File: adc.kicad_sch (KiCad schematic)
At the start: 15 parts, among them U9 ADS8584S

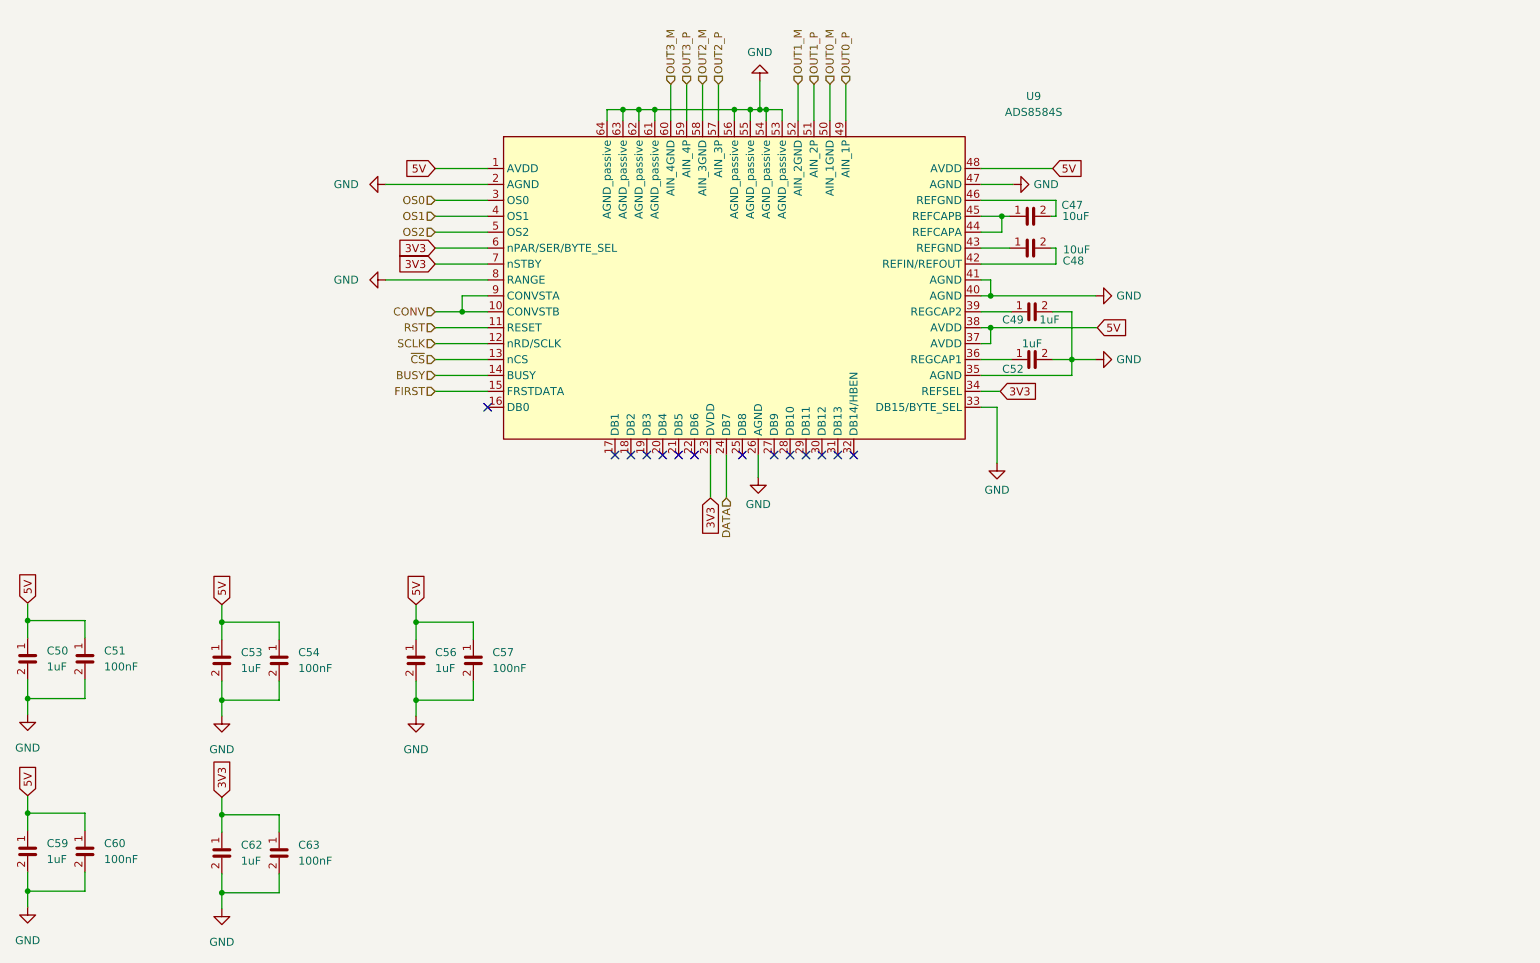
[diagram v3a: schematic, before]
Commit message: Added connector to all sheets.
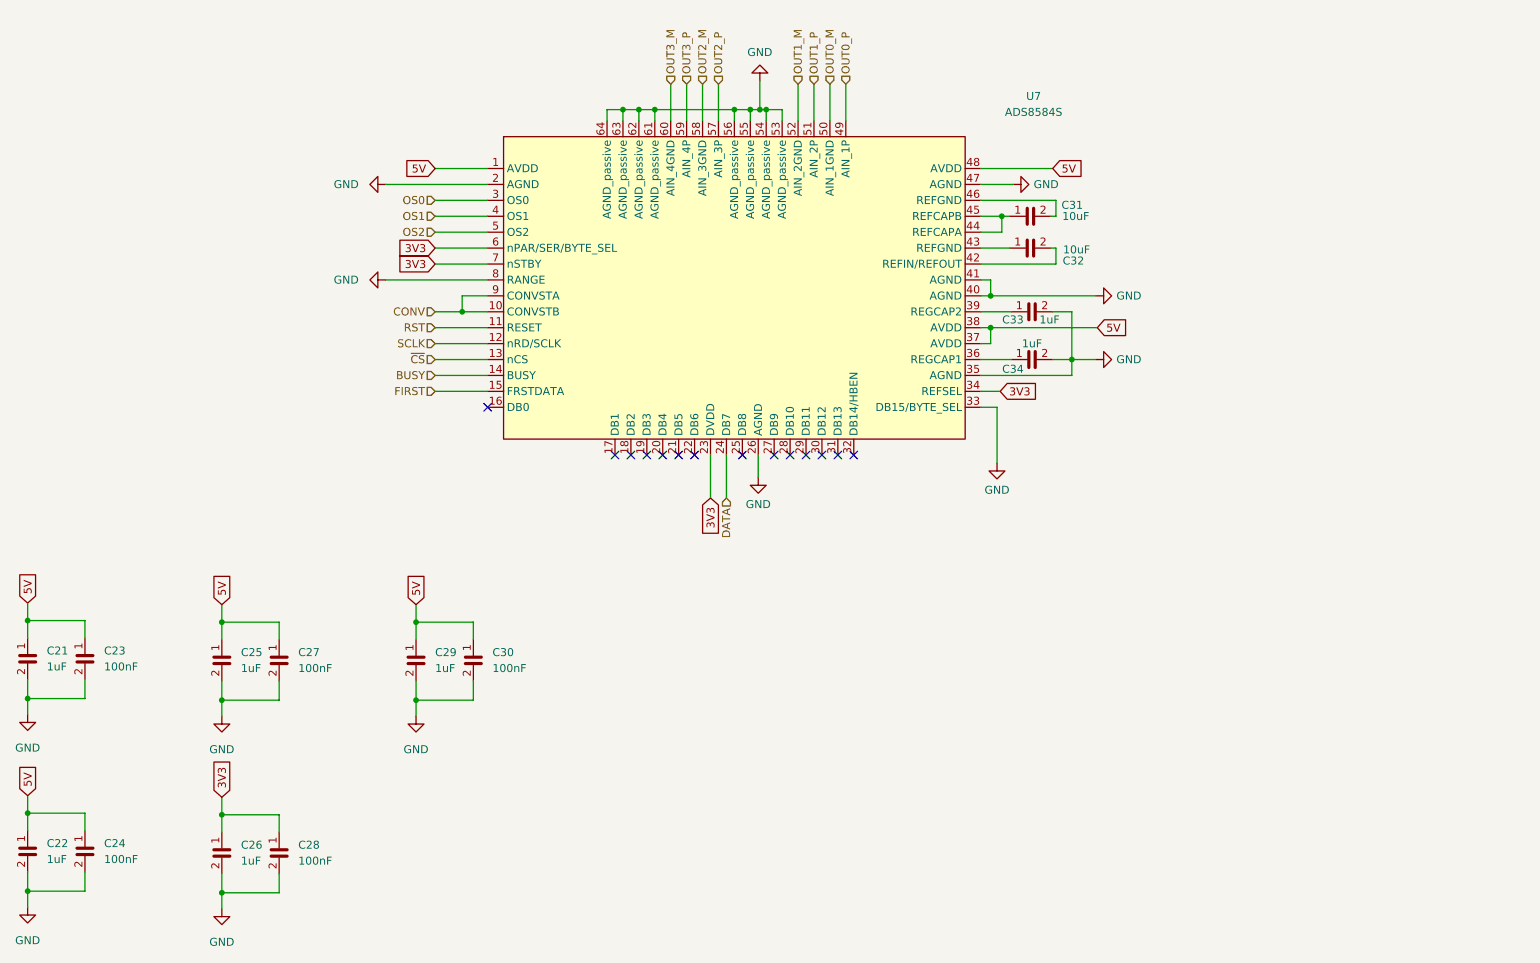
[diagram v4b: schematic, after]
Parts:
- renumbered C50 to C21, C59 to C22, C51 to C23, C60 to C24, C53 to C25, C62 to C26, C54 to C27, C63 to C28, C56 to C29, C57 to C30, C47 to C31, C48 to C32, C49 to C33, C52 to C34, U9 to U7

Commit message: Schematic finished, ready for review.
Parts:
- renumbered U7 to U5
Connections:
- net GND: now also C31.2, C32.2, U5.43 (REFGND), U5.46 (REFGND)
- net at U5.42 (REFIN/REFOUT): now also C32.1; no longer C32.2
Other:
- moved on the sheet: C31, C32

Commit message: Layout erster Entwurf fertig.
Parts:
- removed C29: C0402_1uF_6.3V, Capacitor_SMD:C_0402_1005Metric, symbol Jojos_Lib:C0402_1uF_6.3V
- removed C30: C0402_100nF_50V, Capacitor_SMD:C_0402_1005Metric, symbol Jojos_Lib:C0402_100nF_50V
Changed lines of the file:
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@@
   (junction (at 142.24 62.484) (diameter 0) (color 0 0 0 0)
   )
-  (junction (at 91.44 144.272) (diameter 0) (color 0 0 0 0)
-  )
   (junction (at 146.304 62.484) (diameter 0) (color 0 0 0 0)
   )
@@
   )
   (junction (at 194.818 79.502) (diameter 0) (color 0 0 0 0)
-  )
-  (junction (at 91.44 156.718) (diameter 0) (color 0 0 0 0)
   )
   (junction (at 127 62.484) (diameter 0) (color 0 0 0 0)
@@
     (stroke (width 0) (type default))
   )
-  (wire (pts (xy 91.44 144.272) (xy 91.44 147.066))
-    (stroke (width 0) (type default))
-  )
   (wire (pts (xy 69.596 156.718) (xy 69.596 153.67))
     (stroke (width 0) (type default))
@@
     (stroke (width 0) (type default))
   )
-  (wire (pts (xy 91.44 156.718) (xy 91.44 153.67))
-    (stroke (width 0) (type default))
-  )
   (wire (pts (xy 181.61 84.582) (xy 194.818 84.582))
     (stroke (width 0) (type default))
@@
     (stroke (width 0) (type default))
   )
-  (wire (pts (xy 91.44 156.718) (xy 100.584 156.718))
-    (stroke (width 0) (type default))
-  )
   (wire (pts (xy 181.61 99.822) (xy 183.134 99.822))
     (stroke (width 0) (type default))
@@
     (stroke (width 0) (type default))
   )
-  (wire (pts (xy 91.44 141.478) (xy 91.44 144.272))
-    (stroke (width 0) (type default))
-  )
   (wire (pts (xy 94.488 87.122) (xy 102.87 87.122))
     (stroke (width 0) (type default))
@@
     (stroke (width 0) (type default))
   )
-  (wire (pts (xy 100.584 144.272) (xy 91.44 144.272))
-    (stroke (width 0) (type default))
-  )
   (wire (pts (xy 86.614 74.422) (xy 102.87 74.422))
     (stroke (width 0) (type default))
@@
     (stroke (width 0) (type default))
   )
-  (wire (pts (xy 100.584 156.718) (xy 100.584 153.67))
-    (stroke (width 0) (type default))
-  )
-  (wire (pts (xy 100.584 144.272) (xy 100.584 147.066))
-    (stroke (width 0) (type default))
-  )
   (wire (pts (xy 181.61 109.982) (xy 184.15 109.982))
     (stroke (width 0) (type default))
@@
   )
   (wire (pts (xy 181.61 104.902) (xy 196.088 104.902))
-    (stroke (width 0) (type default))
-  )
-  (wire (pts (xy 91.44 156.718) (xy 91.44 159.258))
     (stroke (width 0) (type default))
   )
@@
     (effects (font (size 1.27 1.27)) (justify left))
     (property "Intersheetrefs" "${INTERSHEET_REFS}" (at 29.464 136.0201 90)
-      (effects (font (size 1.27 1.27)) (justify left) hide)
-    )
-  )
-  (global_label "5V" (shape input) (at 91.44 141.478 90) (fields_autoplaced)
-    (effects (font (size 1.27 1.27)) (justify left))
-    (property "Intersheetrefs" "${INTERSHEET_REFS}" (at 91.44 136.2741 90)
       (effects (font (size 1.27 1.27)) (justify left) hide)
     )
@@
     )
   )
-  (symbol (lib_id "Jojos_Lib:C0402_100nF_50V") (at 100.584 150.368 0) (unit 1)
-    (in_bom yes) (on_board yes) (dnp no) (fields_autoplaced)
-    (property "Reference" "C30" (at 102.87 149.098 0)
-      (effects (font (size 1.27 1.27)) (justify left))
-    )
-    (property "Value" "C0402_100nF_50V" (at 115.062 152.4 0)
-      (effects (font (size 1.27 1.27)) hide)
-    )
-    (property "Footprint" "Capacitor_SMD:C_0402_1005Metric" (at 123.19 148.082 0)
-      (effects (font (size 1.27 1.27)) hide)
-    )
-    (property "Datasheet" "" (at 100.584 150.368 0)
-      (effects (font (size 1.27 1.27)) hide)
-    )
-    (property "Mouser Part Number" "581-04025C104KAT4A" (at 117.348 150.368 0)
-      (effects (font (size 1.27 1.27)) hide)
-    )
-    (property "Place" "Yes" (at 100.584 150.368 0)
-      (effects (font (size 1.27 1.27)) hide)
-    )
-    (property "Val" "100nF" (at 102.87 151.638 0)
-      (effects (font (size 1.27 1.27)) (justify left))
-    )
-    (pin "1")
-    (pin "2")
-    (instances
-      (project "CMEX"
-        (path "/03c4a148-37f4-4d5a-ada3-efb0d725ba7b/006bf3bb-a88e-4438-b530-faa5a7972e5e"
-          (reference "C30") (unit 1)
-        )
-        (path "/03c4a148-37f4-4d5a-ada3-efb0d725ba7b/f0e2f768-e007-42ca-a994-5073588a4ef2"
-          (reference "C37") (unit 1)
-        )
-      )
-    )
-  )
   (symbol (lib_id "power:GND") (at 186.69 74.422 90) (unit 1)
     (in_bom yes) (on_board yes) (dnp no) (fields_autoplaced)
@@
     )
   )
-  (symbol (lib_id "power:GND") (at 91.44 159.258 0) (unit 1)
-    (in_bom yes) (on_board yes) (dnp no) (fields_autoplaced)
-    (property "Reference" "#PWR028" (at 91.44 165.608 0)
-      (effects (font (size 1.27 1.27)) hide)
-    )
-    (property "Value" "GND" (at 91.44 163.068 0)
-      (effects (font (size 1.27 1.27)))
-    )
-    (property "Footprint" "" (at 91.44 159.258 0)
-      (effects (font (size 1.27 1.27)) hide)
-    )
-    (property "Datasheet" "" (at 91.44 159.258 0)
-      (effects (font (size 1.27 1.27)) hide)
-    )
-    (pin "1")
-    (instances
-      (project "CMEX"
-        (path "/03c4a148-37f4-4d5a-ada3-efb0d725ba7b/006bf3bb-a88e-4438-b530-faa5a7972e5e"
-          (reference "#PWR028") (unit 1)
-        )
-        (path "/03c4a148-37f4-4d5a-ada3-efb0d725ba7b/f0e2f768-e007-42ca-a994-5073588a4ef2"
-          (reference "#PWR031") (unit 1)
-        )
-      )
-    )
-  )
   (symbol (lib_id "Jojos_Lib:C0402_1uF_6.3V") (at 189.484 94.742 90) (unit 1)
     (in_bom yes) (on_board yes) (dnp no)
@@
         )
       )
-    )
-  )
-  (symbol (lib_id "Jojos_Lib:C0402_1uF_6.3V") (at 91.44 150.114 0) (unit 1)
-    (in_bom yes) (on_board yes) (dnp no) (fields_autoplaced)
-    (property "Reference" "C29" (at 93.98 149.098 0)
-      (effects (font (size 1.27 1.27)) (justify left))
-    )
-    (property "Value" "C0402_1uF_6.3V" (at 103.886 155.448 0)
-      (effects (font (size 1.27 1.27)) hide)
-    )
-    (property "Footprint" "Capacitor_SMD:C_0402_1005Metric" (at 112.776 147.32 0)
-      (effects (font (size 1.27 1.27)) hide)
-    )
-    (property "Datasheet" "" (at 91.44 150.622 0)
-      (effects (font (size 1.27 1.27)) hide)
-    )
-    (property "Mouser Part Number" "80-C0402C105M9PAC" (at 106.68 150.114 0)
-      (effects (font (size 1.27 1.27)) hide)
-    )
-    (property "Place" "Yes" (at 98.044 152.908 0)
-      (effects (font (size 1.27 1.27)) hide)
-    )
-    (property "Val" "1uF" (at 93.98 151.638 0)
-      (effects (font (size 1.27 1.27)) (justify left))
-    )
-    (pin "1")
-    (pin "2")
-    (instances
-      (project "CMEX"
-        (path "/03c4a148-37f4-4d5a-ada3-efb0d725ba7b/006bf3bb-a88e-4438-b530-faa5a7972e5e"
-          (reference "C29") (unit 1)
-        )
-        (path "/03c4a148-37f4-4d5a-ada3-efb0d725ba7b/f0e2f768-e007-42ca-a994-5073588a4ef2"
-          (reference "C35") (unit 1)
-        )
-      )

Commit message: Kleine Änderung.
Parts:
- added C11: C0402_1uF_6.3V, Capacitor_SMD:C_0402_1005Metric, symbol Jojos_Lib:C0402_1uF_6.3V
- added C12: C0402_100nF_50V, Capacitor_SMD:C_0402_1005Metric, symbol Jojos_Lib:C0402_100nF_50V
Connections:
- net 3V3: now also C11.1, C12.1
- net GND: now also C11.2, C12.2
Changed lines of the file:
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@@
   (junction (at 29.464 144.018) (diameter 0) (color 0 0 0 0)
   )
+  (junction (at 82.55 187.452) (diameter 0) (color 0 0 0 0)
+  )
   (junction (at 183.134 92.202) (diameter 0) (color 0 0 0 0)
   )
@@
   )
   (junction (at 196.088 102.362) (diameter 0) (color 0 0 0 0)
+  )
+  (junction (at 82.55 175.006) (diameter 0) (color 0 0 0 0)
   )
   (junction (at 60.452 187.452) (diameter 0) (color 0 0 0 0)
@@
     (stroke (width 0) (type default))
   )
+  (wire (pts (xy 91.694 175.006) (xy 82.55 175.006))
+    (stroke (width 0) (type default))
+  )
   (wire (pts (xy 121.92 64.262) (xy 121.92 62.484))
     (stroke (width 0) (type default))
@@
     (stroke (width 0) (type default))
   )
+  (wire (pts (xy 82.55 175.006) (xy 82.55 177.8))
+    (stroke (width 0) (type default))
+  )
   (wire (pts (xy 94.488 71.882) (xy 102.87 71.882))
     (stroke (width 0) (type default))
@@
     (stroke (width 0) (type default))
   )
+  (wire (pts (xy 82.55 187.452) (xy 91.694 187.452))
+    (stroke (width 0) (type default))
+  )
   (wire (pts (xy 60.452 187.452) (xy 60.452 184.404))
     (stroke (width 0) (type default))
@@
     (stroke (width 0) (type default))
   )
+  (wire (pts (xy 91.694 177.8) (xy 91.694 175.006))
+    (stroke (width 0) (type default))
+  )
   (wire (pts (xy 60.452 156.718) (xy 60.452 159.258))
     (stroke (width 0) (type default))
@@
     (stroke (width 0) (type default))
   )
+  (wire (pts (xy 82.55 187.452) (xy 82.55 189.992))
+    (stroke (width 0) (type default))
+  )
   (wire (pts (xy 181.61 109.982) (xy 184.15 109.982))
     (stroke (width 0) (type default))
@@
     (stroke (width 0) (type default))
   )
+  (wire (pts (xy 91.694 187.452) (xy 91.694 184.404))
+    (stroke (width 0) (type default))
+  )
   (wire (pts (xy 196.088 94.742) (xy 196.088 102.362))
     (stroke (width 0) (type default))
@@
     (stroke (width 0) (type default))
   )
+  (wire (pts (xy 82.55 187.452) (xy 82.55 184.404))
+    (stroke (width 0) (type default))
+  )
   (wire (pts (xy 38.608 146.812) (xy 38.608 144.018))
+    (stroke (width 0) (type default))
+  )
+  (wire (pts (xy 82.55 172.212) (xy 82.55 175.006))
     (stroke (width 0) (type default))
   )
@@
     (effects (font (size 1.27 1.27)) (justify left))
     (property "Intersheetrefs" "${INTERSHEET_REFS}" (at 29.464 136.0201 90)
+      (effects (font (size 1.27 1.27)) (justify left) hide)
+    )
+  )
+  (global_label "3V3" (shape input) (at 82.55 172.212 90) (fields_autoplaced)
+    (effects (font (size 1.27 1.27)) (justify left))
+    (property "Intersheetrefs" "${INTERSHEET_REFS}" (at 82.55 165.7986 90)
       (effects (font (size 1.27 1.27)) (justify left) hide)
     )
@@
     )
   )
+  (symbol (lib_id "Jojos_Lib:C0402_1uF_6.3V") (at 82.55 180.848 0) (unit 1)
+    (in_bom yes) (on_board yes) (dnp no) (fields_autoplaced)
+    (property "Reference" "C11" (at 85.598 179.832 0)
+      (effects (font (size 1.27 1.27)) (justify left))
+    )
+    (property "Value" "C0402_1uF_6.3V" (at 94.996 186.182 0)
+      (effects (font (size 1.27 1.27)) hide)
+    )
+    (property "Footprint" "Capacitor_SMD:C_0402_1005Metric" (at 103.886 178.054 0)
+      (effects (font (size 1.27 1.27)) hide)
+    )
+    (property "Datasheet" "" (at 82.55 181.356 0)
+      (effects (font (size 1.27 1.27)) hide)
+    )
+    (property "Mouser Part Number" "80-C0402C105M9PAC" (at 97.79 180.848 0)
+      (effects (font (size 1.27 1.27)) hide)
+    )
+    (property "Place" "Yes" (at 89.154 183.642 0)
+      (effects (font (size 1.27 1.27)) hide)
+    )
+    (property "Val" "1uF" (at 85.598 182.372 0)
+      (effects (font (size 1.27 1.27)) (justify left))
+    )
+    (pin "1")
+    (pin "2")
+    (instances
+      (project "CMEX"
+        (path "/03c4a148-37f4-4d5a-ada3-efb0d725ba7b/006bf3bb-a88e-4438-b530-faa5a7972e5e"
+          (reference "C11") (unit 1)
+        )
+        (path "/03c4a148-37f4-4d5a-ada3-efb0d725ba7b/f0e2f768-e007-42ca-a994-5073588a4ef2"
+          (reference "C29") (unit 1)
+        )
+      )
+    )
+  )
   (symbol (lib_id "power:GND") (at 29.464 189.738 0) (unit 1)
     (in_bom yes) (on_board yes) (dnp no) (fields_autoplaced)
@@
         (path "/03c4a148-37f4-4d5a-ada3-efb0d725ba7b/006bf3bb-a88e-4438-b530-faa5a7972e5e"
           (reference "#PWR029") (unit 1)
+        )
+      )
+    )
+  )
+  (symbol (lib_id "power:GND") (at 82.55 189.992 0) (unit 1)
+    (in_bom yes) (on_board yes) (dnp no) (fields_autoplaced)
+    (property "Reference" "#PWR015" (at 82.55 196.342 0)
+      (effects (font (size 1.27 1.27)) hide)
+    )
+    (property "Value" "GND" (at 82.55 193.802 0)
+      (effects (font (size 1.27 1.27)))
+    )
+    (property "Footprint" "" (at 82.55 189.992 0)
+      (effects (font (size 1.27 1.27)) hide)
+    )
+    (property "Datasheet" "" (at 82.55 189.992 0)
+      (effects (font (size 1.27 1.27)) hide)
+    )
+    (pin "1")
+    (instances
+      (project "CMEX"
+        (path "/03c4a148-37f4-4d5a-ada3-efb0d725ba7b/006bf3bb-a88e-4438-b530-faa5a7972e5e"
+          (reference "#PWR015") (unit 1)
+        )
+        (path "/03c4a148-37f4-4d5a-ada3-efb0d725ba7b/f0e2f768-e007-42ca-a994-5073588a4ef2"
+          (reference "#PWR027") (unit 1)
         )
       )
@@
         )
       )
+    )
+  )
+  (symbol (lib_id "Jojos_Lib:C0402_100nF_50V") (at 91.694 181.102 0) (unit 1)
+    (in_bom yes) (on_board yes) (dnp no) (fields_autoplaced)
+    (property "Reference" "C12" (at 94.488 179.832 0)
+      (effects (font (size 1.27 1.27)) (justify left))
+    )
+    (property "Value" "C0402_100nF_50V" (at 106.172 183.134 0)
+      (effects (font (size 1.27 1.27)) hide)
+    )
+    (property "Footprint" "Capacitor_SMD:C_0402_1005Metric" (at 114.3 178.816 0)
+      (effects (font (size 1.27 1.27)) hide)
+    )
+    (property "Datasheet" "" (at 91.694 181.102 0)
+      (effects (font (size 1.27 1.27)) hide)
+    )
+    (property "Mouser Part Number" "581-04025C104KAT4A" (at 108.458 181.102 0)
+      (effects (font (size 1.27 1.27)) hide)
+    )
+    (property "Place" "Yes" (at 91.694 181.102 0)
+      (effects (font (size 1.27 1.27)) hide)
+    )
+    (property "Val" "100nF" (at 94.488 182.372 0)
+      (effects (font (size 1.27 1.27)) (justify left))
+    )
+    (pin "1")
+    (pin "2")
+    (instances
+      (project "CMEX"
+        (path "/03c4a148-37f4-4d5a-ada3-efb0d725ba7b/006bf3bb-a88e-4438-b530-faa5a7972e5e"
+          (reference "C12") (unit 1)
+        )
+        (path "/03c4a148-37f4-4d5a-ada3-efb0d725ba7b/f0e2f768-e007-42ca-a994-5073588a4ef2"
+          (reference "C31") (unit 1)
+        )
+      )
